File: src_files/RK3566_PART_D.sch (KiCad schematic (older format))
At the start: 16 parts

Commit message: littleupdate
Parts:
- removed U?: RK3566, symbol GCL_Integrated-Circuits:RK3566
- added C84, C85: 18pF, Capacitor_SMD:C_0402_1005Metric, symbol Device:C_Small
- added C86, C93: 100nF, Capacitor_SMD:C_0402_1005Metric, symbol Device:C_Small
- added R20, R21: 0R, Resistor_SMD:R_0402_1005Metric, symbol Device:R_US
- added U1: RK3566, greencharge-footprints:BGA828C65P31X31_2100X2100X161N, symbol GCL_Integrated-Circuits:RK3566
- added Y3: 24MHz/10ppm, Crystal:Crystal_SMD_3225-4Pin_3.2x2.5mm_HandSoldering, symbol Device:Crystal_GND24_Small
- C87, C88, C89, C90, C91, C92, C94, C95, C96, C97, C98: renamed from C?; footprint (none) -> Capacitor_SMD:C_0402_1005Metric
- R22, R23, R24: renamed from R?; footprint (none) -> Resistor_SMD:R_0402_1005Metric
- gave numbers to parts that had none: 1
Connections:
- net GND: now also C84.2, C85.2, C86.2, C93.2, U1.1D4 (DDR_AVSS), Y3.2, Y3.4
- net LPDDR4_A0_A: now also U1.C2 (LPDDR4_A0_A)
- net LPDDR4_A0_B: now also U1.A9 (LPDDR4_A0_B)
- net LPDDR4_A1_A: now also U1.C1 (LPDDR4_A1_A)
- net LPDDR4_A1_B: now also U1.B9 (LPDDR4_A1_B)
- net LPDDR4_A2_A: now also U1.1C1 (LPDDR4_A2_A)
- net LPDDR4_A2_B: now also U1.1B7 (LPDDR4_A2_B)
- net LPDDR4_A3_A: now also U1.1B3 (LPDDR4_A3_A)
- net LPDDR4_A3_B: now also U1.1B6 (LPDDR4_A3_B)
- net LPDDR4_A4_A: now also U1.1B1 (LPDDR4_A4_A)
- net LPDDR4_A4_B: now also U1.1A6 (LPDDR4_A4_B)
- net LPDDR4_A5_A: now also U1.1A1 (LPDDR4_A5_A)
- net LPDDR4_A5_B: now also U1.B8 (LPDDR4_A5_B)
- net LPDDR4_CKE0_A: now also U1.B4 (LPDDR4_CKE0_A)
- net LPDDR4_CKE0_B: now also U1.1A3 (LPDDR4_CKE0_B)
- net LPDDR4_CKE1_A: now also U1.1C3 (LPDDR4_CKE1)
- net LPDDR4_CKE1_B: now also U1.1A2 (LPDDR4_CKE1_B)
- net LPDDR4_CLKN_A: now also U1.A5 (LPDDR4_CLKN_A)
- net LPDDR4_CLKN_B: now also U1.B7 (LPDDR4_CLKN_B)
- net LPDDR4_CLKP_A: now also U1.B5 (LPDDR4_CLKP_A)
- net LPDDR4_CLKP_B: now also U1.A7 (LPDDR4_CLKP_B)
- net LPDDR4_CS0n_A: now also U1.B3 (LPDDR4_CS0n_A)
- net LPDDR4_CS0n_B: now also U1.1B5 (LPDDR4_CS0n_B)
- net LPDDR4_CS1n_A: now also U1.A3 (LPDDR4_CS1n_A)
- net LPDDR4_CS1n_B: now also U1.1A5 (LPDDR4_CS1n_B)
- net LPDDR4_DM0_A: now also U1.1E2 (LPDDR4_DM0_A)
- net LPDDR4_DM0_B: now also U1.1B8 (LPDDR4_DM0_B)
- net LPDDR4_DM1_A: now also U1.1G1 (LPDDR4_DM1_A)
- net LPDDR4_DM1_B: now also U1.1A11 (LPDDR4_DM1_B)
- net LPDDR4_DQ0_A: now also U1.G2 (DDR_DQ0_A/DDR4_DQL0_A/LPDDR4_DQ0_A/DDR3_DQ0/LPDDR3_DQ15)
- net LPDDR4_DQ0_B: now also U1.B12 (LPDDR4_DQ0_B)
- net LPDDR4_DQ10_A: now also U1.R2 (LPDDR4_DQ10_A)
- net LPDDR4_DQ10_B: now also U1.A20 (LPDDR4_DQ10_B)
- net LPDDR4_DQ11_A: now also U1.T2 (LPDDR4_DQ11_A)
- net LPDDR4_DQ11_B: now also U1.B20 (LPDDR4_DQ11_B)
- net LPDDR4_DQ12_A: now also U1.M1 (LPDDR4_DQ12_A)
- net LPDDR4_DQ12_B: now also U1.A15 (LPDDR4_DQ12_B)
- net LPDDR4_DQ13_A: now also U1.1F2 (LPDDR4_DQ13_A)
- net LPDDR4_DQ13_B: now also U1.B15 (LPDDR4_DQ13_B)
- net LPDDR4_DQ14_A: now also U1.1F1 (LPDDR4_DQ14_A)
- net LPDDR4_DQ14_B: now also U1.1C10 (LPDDR4_DQ14_B)
- net LPDDR4_DQ15_A: now also U1.1G2 (LPDDR4_DQ15_A)
- net LPDDR4_DQ15_B: now also U1.B16 (LPDDR4_DQ15_B)
- net LPDDR4_DQ1_A: now also U1.F2 (DDR_DQ1_A/DDR4_DQL2_A/LPDDR4_DQ1_A/DDR3_DQ1/LPDDR3_DQ14)
- net LPDDR4_DQ1_B: now also U1.B10 (LPDDR4_DQ1_B)
- net LPDDR4_DQ2_A: now also U1.F1 (DDR_DQ2_A/DDR4_DQL4_A/LPDDR4_DQ2_A/DDR3_DQ2/LPDDR3_DQ10)
- net LPDDR4_DQ2_B: now also U1.1A8 (LPDDR4_DQ2_B)
- net LPDDR4_DQ3_A: now also U1.E1 (DDR_DQ3_A/DDR4_DQL6_A//_LPDDR4_DQ3_A/DDR3_DQ3/LPDDR3_DQ9)
- net LPDDR4_DQ3_B: now also U1.1A7 (LPDDR4_DQ3_B)
- net LPDDR4_DQ4_A: now also U1.M2 (LPDDR4_DQ4_A)
- net LPDDR4_DQ4_B: now also U1.B13 (LPDDR4_DQ4_B)
- net LPDDR4_DQ5_A: now also U1.K1 (LPDDR4_DQ5_A)
- net LPDDR4_DQ5_B: now also U1.1A10 (LPDDR4_DQ5_B)
- net LPDDR4_DQ6_A: now also U1.K2 (LPDDR4_DQ6_A)
- net LPDDR4_DQ6_B: now also U1.1B9 (LPDDR4_DQ6_B)
- net LPDDR4_DQ7_A: now also U1.1E1 (LPDDR4_DQ7_A)
- net LPDDR4_DQ7_B: now also U1.1A9 (LPDDR4_DQ7_B)
- net LPDDR4_DQ8_A: now also U1.P2 (LPDDR4_DQ8_A)
- net LPDDR4_DQ8_B: now also U1.B19 (LPDDR4_DQ8_B)
- net LPDDR4_DQ9_A: now also U1.R1 (LPDDR4_DQ9_A)
- net LPDDR4_DQ9_B: now also U1.A19 (LPDDR4_DQ9_B)
- net LPDDR4_DQS0N_A: now also U1.H1 (LPDDR4_DQS0N_A)
- net LPDDR4_DQS0N_B: now also U1.A12 (LPDDR4_DQS0N_B)
- net LPDDR4_DQS0P_A: now also U1.H2 (LPDDR4_DQS0P_A)
- net LPDDR4_DQS0P_B: now also U1.A13 (LPDDR4_DQS0P_B)
- net LPDDR4_DQS1N_A: now also U1.N2 (LPDDR4_DQS1N_A)
- net LPDDR4_DQS1N_B: now also U1.B17 (LPDDR4_DQS1N_B)
- net LPDDR4_DQS1P_A: now also U1.N1 (LPDDR4_DQS1P_A)
- net LPDDR4_DQS1P_B: now also U1.A17 (LPDDR4_DQS1P_B)
- net LPDDR4_ODT0_CA_A: now also U1.E2 (LPDDR4_ODT0_CA_A)
- net LPDDR4_ODT0_CA_B: now also U1.A10 (LPDDR4_ODT0_CA_B)
- net LPDDR4_RESETn: now also U1.1C7 (LPDDR4_RESETn)
- net VCC_DDR: now also U1.1D5 (DDR_VDDQ_1), U1.1D6 (DDR_VDDQ_2), U1.1D7 (DDR_VDDQ_3), U1.1D8 (DDR_VDDQ_4), U1.1D9 (DDR_VDDQ_5), U1.1E4 (DDR_VDDQ_6), U1.1E6 (DDR_VDDQL_1), U1.1E7 (DDR_VDDQL_2), U1.1E9 (DDR_VDDQL_3), U1.1F4 (DDR_VDDQ_7), U1.1F5 (DDR_VDDQL_4), U1.1G4 (DDR_VDDQ_8), U1.1G5 (DDR_VDDQL_5)
- net at R22.2: now also U1.1F3 (DDR_RZQ)
- new net: C85.1, U1.AD37 (XIN24M), Y3.1
- new net: C84.1, U1.AD38 (XOUT24M), Y3.3
- new net: R20.1, U1.1M18 (TVSS)
- new net: R21.2, U1.1R20 (GPIO0_A1_z)
- new net GMAC1_RSTn_GPIO0_B7: U1.1R17 (GPIO0_B7_d)
- new net I2C0_SCL_PMIC: U1.AJ37 (GPIO0_B1_u)
- new net I2C0_SDA_PMIC: U1.AK38 (GPIO0_B2_u)
- new net I2C1_SCL: U1.AK37 (GPIO0_B3_u)
- new net I2C1_SDA: U1.AM38 (GPIO0_B4_u)
- new net I2C2_SCL_M0_TP: U1.1U20 (GPIO0_B5_u)
- new net I2C2_SDA_M0_TP: U1.1R16 (GPIO0_B6_u)
- new net PMIC_32KOUT_SOC: U1.1T20 (GPIO0_B0_u)
- new net PMIC_INT_L: U1.1R19 (GPIO0_A3_u)
- new net PMIC_SLEEP_H: U1.1P19 (GPIO0_A2_d)
- new net RESETn: C86.1, R21.1, U1.AG38 (nPOR_u)
- new net SDMMC0_DET_L: U1.AF37 (GPIO0_A4_u)
- new net TP_INT_GPIO0_A5: U1.AG37 (GPIO0_A5_d)
- new net USB_HOST5V_EN: U1.AJ38 (GPIO0_A6_d)
- new net VCC3V3_PMU: C93.1, U1.1P16 (PMUIO1)

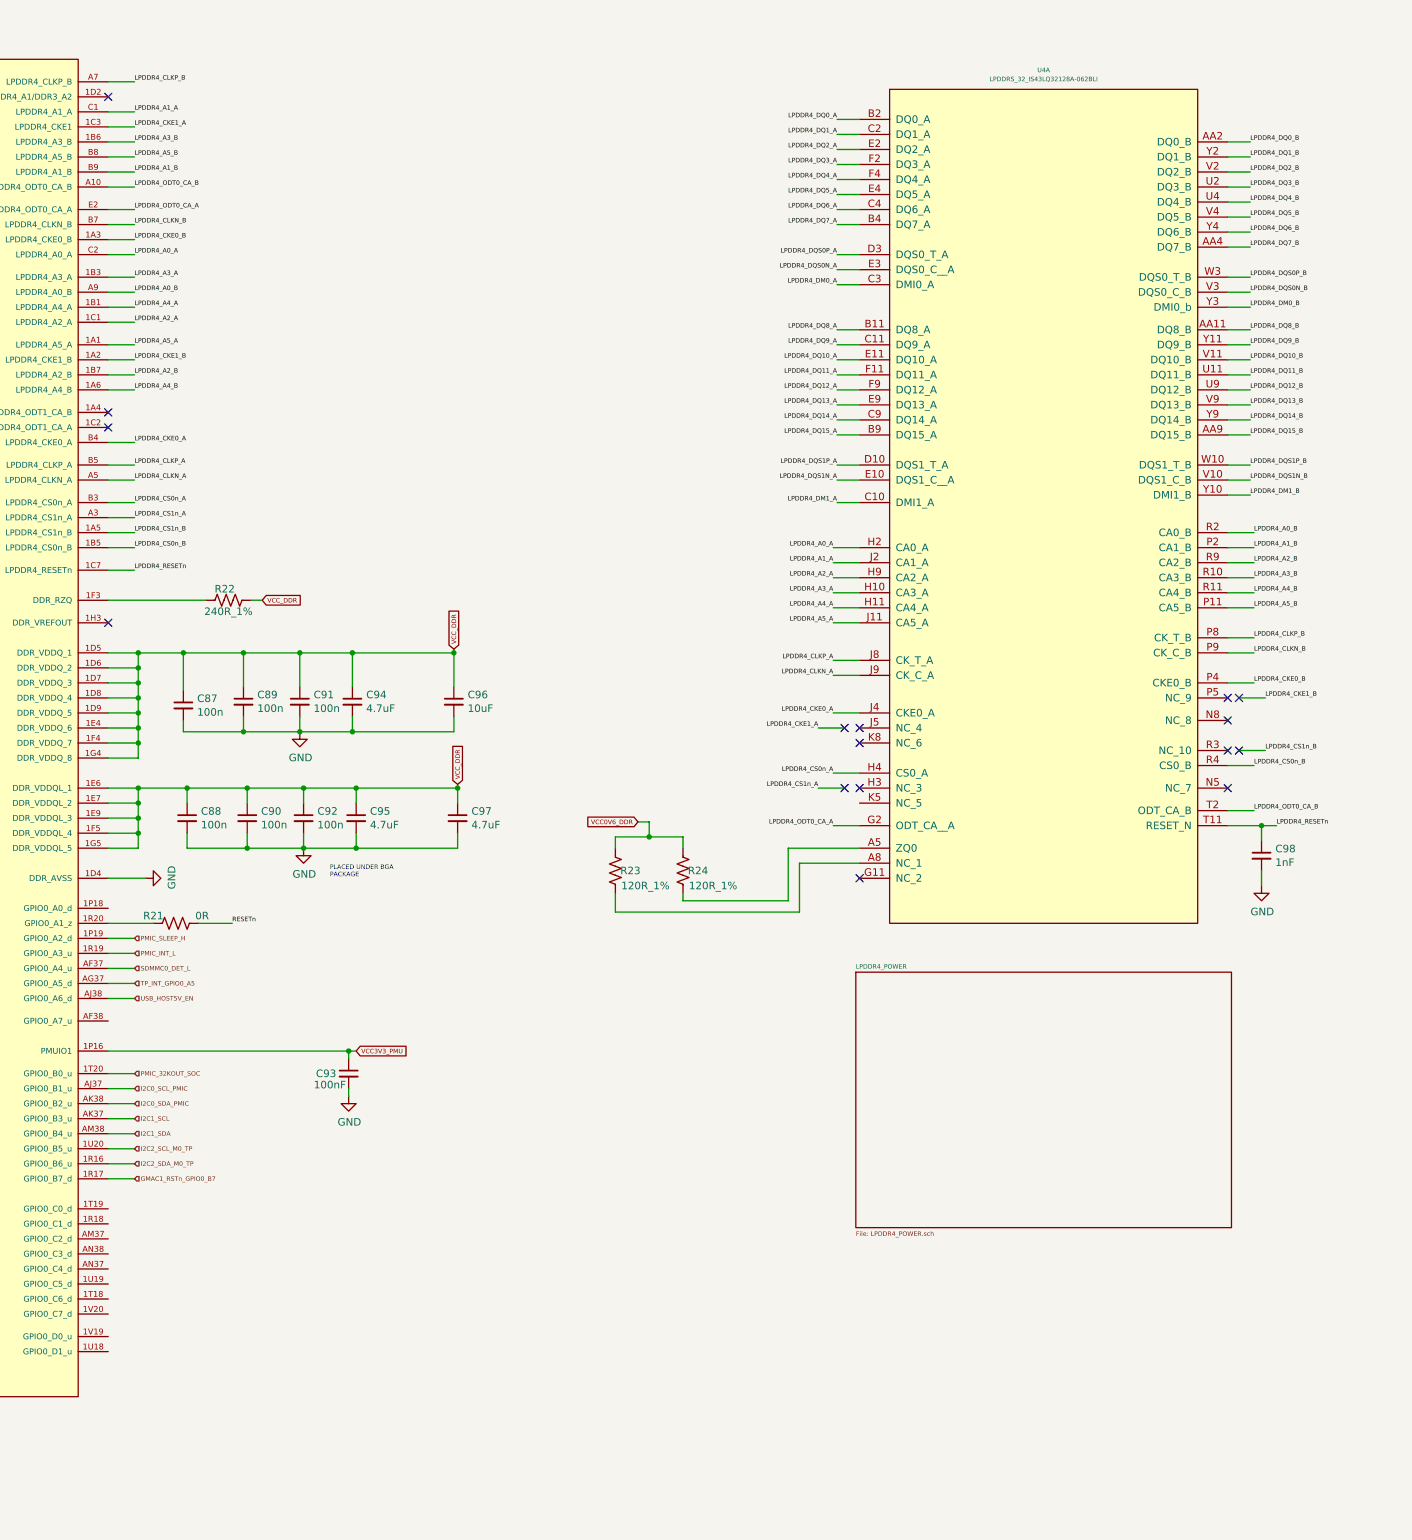
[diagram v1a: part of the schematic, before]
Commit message: added 3 screens
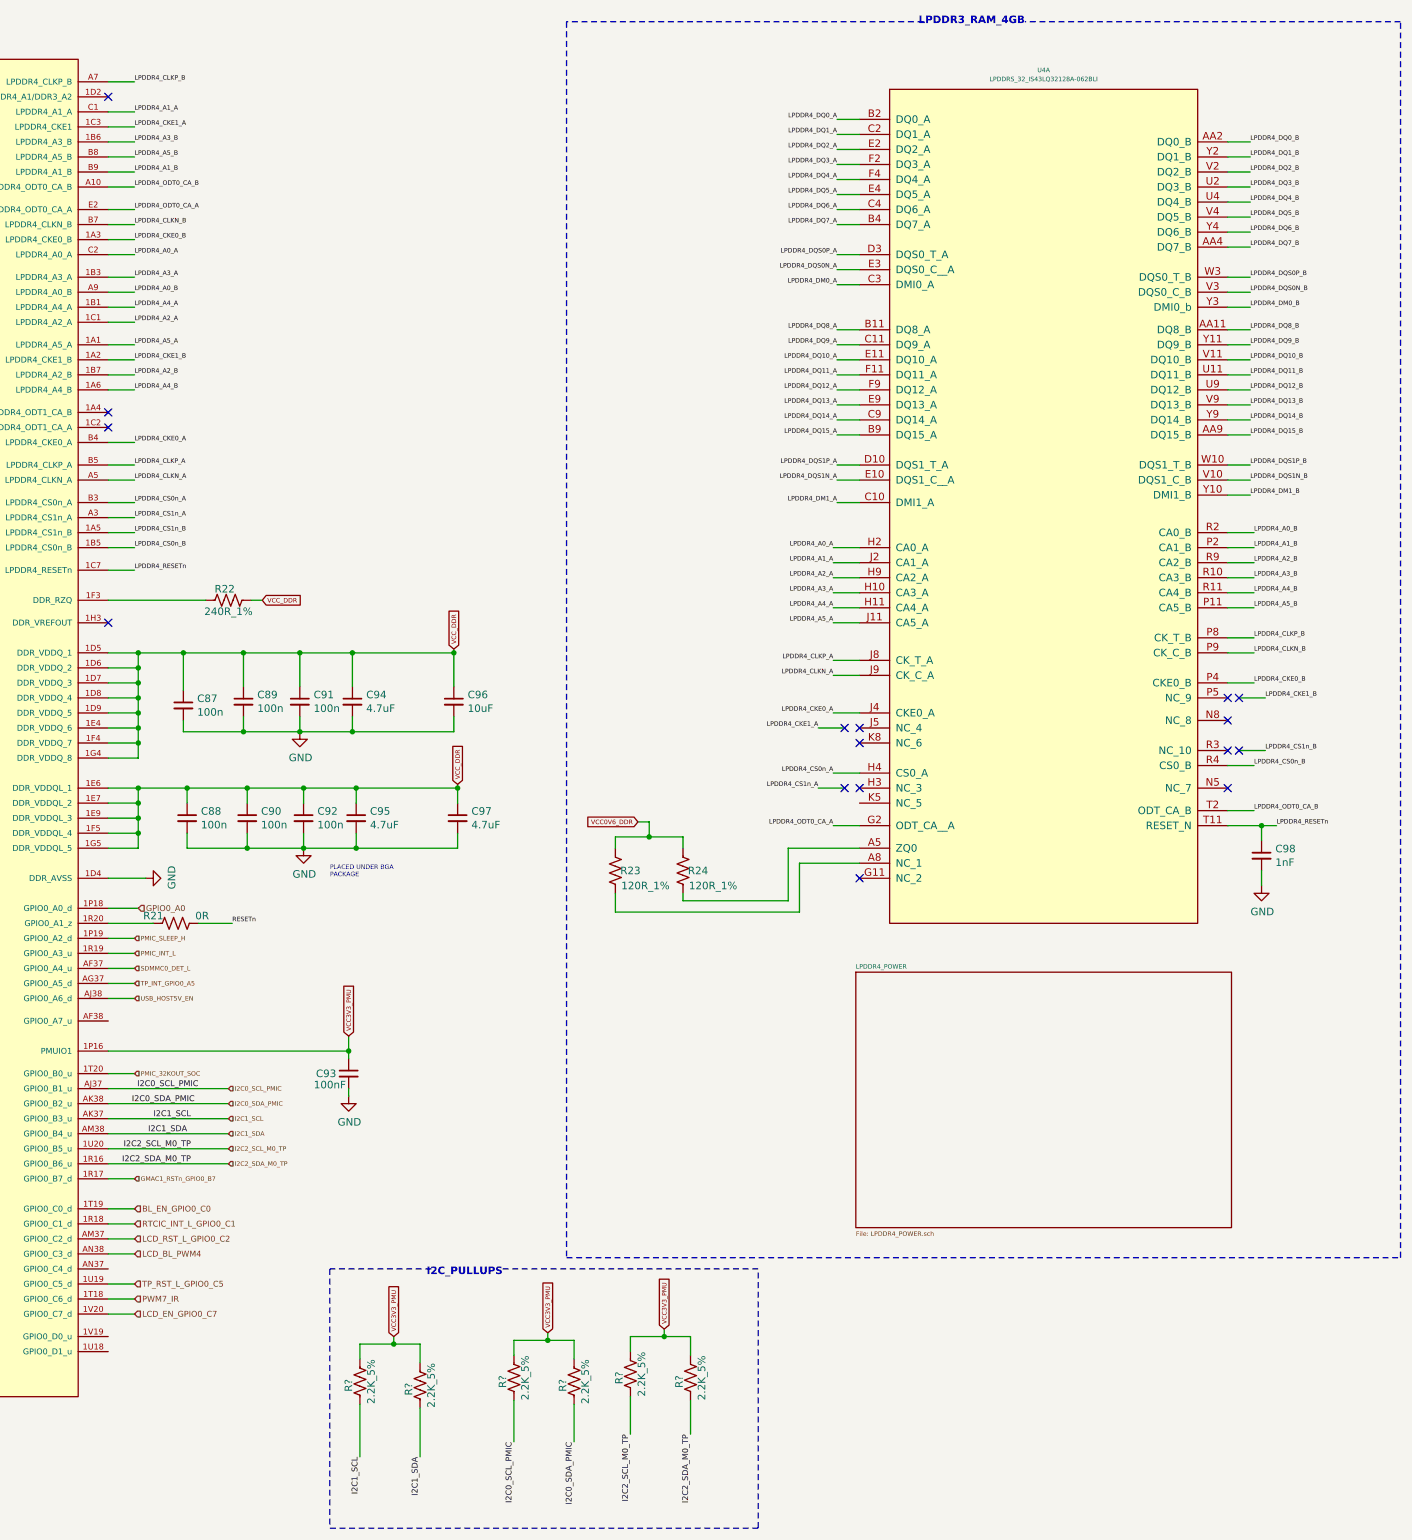
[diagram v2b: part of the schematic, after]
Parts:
- added R? (x6): 2.2K_5%, Resistor_SMD:R_0402_1005Metric, symbol Device:R_US
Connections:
- net I2C0_SCL_PMIC: now also R?.2
- net I2C0_SDA_PMIC: now also R?.2
- net I2C1_SCL: now also R?.2
- net I2C1_SDA: now also R?.2
- net I2C2_SCL_M0_TP: now also R?.2
- net I2C2_SDA_M0_TP: now also R?.2
- net VCC3V3_PMU: now also R?.1, R?.1, R?.1, R?.1, R?.1, R?.1
- net GPIO0_A0: now reaches U1.1P18 (GPIO0_A0_d)
- net RTCIC_INT_L_GPIO0_C1: now reaches U1.1R18 (GPIO0_C1_d)
- net PWM7_IR: now reaches U1.1T18 (GPIO0_C6_d)
- net BL_EN_GPIO0_C0: now reaches U1.1T19 (GPIO0_C0_d)
- net TP_RST_L_GPIO0_C5: now reaches U1.1U19 (GPIO0_C5_d)
- net LCD_EN_GPIO0_C7: now reaches U1.1V20 (GPIO0_C7_d)
- net LCD_RST_L_GPIO0_C2: now reaches U1.AM37 (GPIO0_C2_d)
- net LCD_BL_PWM4: now reaches U1.AN38 (GPIO0_C3_d)
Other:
- note added: "I2C_PULLUPS"
- note added: "LPDDR3_RAM_4GB"
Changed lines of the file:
@@
 $Descr A3 16535 11693
 encoding utf-8
-Sheet 8 11
+Sheet 10 11
 Title ""
 Date ""
@@
 Text HLabel 7425 7550 2    30   Input ~ 0
 USB_HOST5V_EN
-Text GLabel 8900 7900 2    30   Input ~ 0
+Text GLabel 8850 7800 1    30   Input ~ 0
 VCC3V3_PMU
-$Comp
-L Device:C_Small C93
-U 1 1 6340D3E8
-P 8850 8050
-F 0 "C93" H 8700 8050 50  0000 C CNN
-F 1 "100nF" H 8725 7975 50  0000 C CNN
-F 2 "Capacitor_SMD:C_0402_1005Metric" H 8850 8050 50  0001 C CNN
-F 3 "~" H 8850 8050 50  0001 C CNN
-	1    8850 8050
-	1    0    0    -1
-$EndComp
 $Comp
 L OLIMEX_Power:GND #PWR0191
@@
 	8850 8200 8850 8150
 Wire Wire Line
-	8850 7900 8900 7900
-Wire Wire Line
 	8850 7950 8850 7900
 Wire Wire Line
@@
 Text HLabel 7425 8050 2    30   Input ~ 0
 PMIC_32KOUT_SOC
-Text HLabel 7425 8150 2    30   Input ~ 0
+Text HLabel 8050 8150 2    30   Input ~ 0
 I2C0_SCL_PMIC
-Text HLabel 7425 8250 2    30   Input ~ 0
+Text HLabel 8050 8250 2    30   Input ~ 0
 I2C0_SDA_PMIC
-Text HLabel 7425 8350 2    30   Input ~ 0
+Text HLabel 8050 8350 2    30   Input ~ 0
 I2C1_SCL
-Text HLabel 7425 8450 2    30   Input ~ 0
+Text HLabel 8050 8450 2    30   Input ~ 0
 I2C1_SDA
-Text HLabel 7425 8550 2    30   Input ~ 0
-I2C2_SCL_M0_TP
-Text HLabel 7425 8650 2    30   Input ~ 0
-I2C2_SDA_M0_TP
 Text HLabel 7425 8750 2    30   Input ~ 0
 GMAC1_RSTn_GPIO0_B7
 Wire Wire Line
-	7425 8750 7250 8750
-Wire Wire Line
-	7425 8650 7250 8650
-Wire Wire Line
-	7425 8550 7250 8550
-Wire Wire Line
-	7425 8450 7250 8450
-Wire Wire Line
-	7425 8350 7250 8350
-Wire Wire Line
-	7425 8250 7250 8250
-Wire Wire Line
-	7425 8150 7250 8150
+	7425 8950 7250 8950
+Wire Wire Line
+	8050 8450 7250 8450
+Wire Wire Line
+	8050 8350 7250 8350
+Wire Wire Line
+	8050 8250 7250 8250
+Wire Wire Line
+	8050 8150 7250 8150
 Wire Wire Line
 	7425 8050 7250 8050
@@
 	1    0    0    -1
 $EndComp
+Text HLabel 7450 6950 2    39   Input ~ 0
+GPIO0_A0
+Wire Wire Line
+	7450 6950 7250 6950
+Text HLabel 7425 9650 2    39   Input ~ 0
+LCD_EN_GPIO0_C7
+Wire Wire Line
+	7250 9650 7425 9650
+Text HLabel 7425 8950 2    39   Input ~ 0
+BL_EN_GPIO0_C0
+Wire Wire Line
+	7425 8750 7250 8750
+Text HLabel 7425 9250 2    39   Input ~ 0
+LCD_BL_PWM4
+Text HLabel 7425 9150 2    39   Input ~ 0
+LCD_RST_L_GPIO0_C2
+Text HLabel 7425 9050 2    39   Input ~ 0
+RTCIC_INT_L_GPIO0_C1
+Wire Wire Line
+	7425 9050 7250 9050
+Wire Wire Line
+	7425 9150 7250 9150
+Wire Wire Line
+	7425 9250 7250 9250
+Text HLabel 7425 9450 2    39   Input ~ 0
+TP_RST_L_GPIO0_C5
+Text HLabel 7425 9550 2    39   Input ~ 0
+PWM7_IR
+Wire Wire Line
+	7425 9450 7250 9450
+Wire Wire Line
+	7425 9550 7250 9550
+Wire Wire Line
+	8850 7800 8850 7900
+$Comp
+L Device:C_Small C93
+U 1 1 6340D3E8
+P 8850 8050
+F 0 "C93" H 8700 8050 50  0000 C CNN
+F 1 "100nF" H 8725 7975 50  0000 C CNN
+F 2 "Capacitor_SMD:C_0402_1005Metric" H 8850 8050 50  0001 C CNN
+F 3 "~" H 8850 8050 50  0001 C CNN
+	1    8850 8050
+	1    0    0    -1
+$EndComp
+Wire Wire Line
+	9325 9850 9325 9975
+Wire Wire Line
+	8925 9950 8925 9850
+$Comp
+L Device:R_US R?
+U 1 1 6243D32E
+P 9325 10125
+F 0 "R?" V 9250 10100 50  0000 C CNN
+F 1 "2.2K_5%" V 9400 10125 50  0000 C CNN
+F 2 "Resistor_SMD:R_0402_1005Metric" V 9365 10115 50  0001 C CNN
+F 3 "~" H 9325 10125 50  0001 C CNN
+	1    9325 10125
+	1    0    0    -1
+$EndComp
+$Comp
+L Device:R_US R?
+U 1 1 62422541
+P 8925 10100
+F 0 "R?" V 8850 10075 50  0000 C CNN
+F 1 "2.2K_5%" V 9000 10100 50  0000 C CNN
+F 2 "Resistor_SMD:R_0402_1005Metric" V 8965 10090 50  0001 C CNN
+F 3 "~" H 8925 10100 50  0001 C CNN
+	1    8925 10100
+	1    0    0    -1
+$EndComp
+Wire Wire Line
+	8925 9850 9150 9850
+Text GLabel 9150 9800 1    30   Input ~ 0
+VCC3V3_PMU
+Wire Wire Line
+	9325 10275 9325 10600
+Wire Wire Line
+	8925 10250 8925 10600
+Wire Wire Line
+	8050 8550 7250 8550
+Wire Wire Line
+	8050 8650 7250 8650
+Text HLabel 8050 8650 2    30   Input ~ 0
+I2C2_SDA_M0_TP
+Text HLabel 8050 8550 2    30   Input ~ 0
+I2C2_SCL_M0_TP
+Text Label 7850 8150 2    39   ~ 0
+I2C0_SCL_PMIC
+Text Label 7825 8250 2    39   ~ 0
+I2C0_SDA_PMIC
+Text Label 7800 8350 2    39   ~ 0
+I2C1_SCL
+Text Label 7775 8450 2    39   ~ 0
+I2C1_SDA
+Text Label 7800 8550 2    39   ~ 0
+I2C2_SCL_M0_TP
+Text Label 7800 8650 2    39   ~ 0
+I2C2_SDA_M0_TP
+Text Label 11125 10450 3    39   ~ 0
+I2C2_SDA_M0_TP
+Text Label 10725 10450 3    39   ~ 0
+I2C2_SCL_M0_TP
+Text Label 9325 10600 3    39   ~ 0
+I2C1_SDA
+Text Label 8925 10600 3    39   ~ 0
+I2C1_SCL
+Wire Wire Line
+	10350 9825 10350 9950
+Wire Wire Line
+	9950 9925 9950 9825
+$Comp
+L Device:R_US R?
+U 1 1 626F2B0D
+P 10350 10100
+F 0 "R?" V 10275 10075 50  0000 C CNN
+F 1 "2.2K_5%" V 10425 10100 50  0000 C CNN
+F 2 "Resistor_SMD:R_0402_1005Metric" V 10390 10090 50  0001 C CNN
+F 3 "~" H 10350 10100 50  0001 C CNN
+	1    10350 10100
+	1    0    0    -1
+$EndComp
+$Comp
+L Device:R_US R?
+U 1 1 626F2B17
+P 9950 10075
+F 0 "R?" V 9875 10050 50  0000 C CNN
+F 1 "2.2K_5%" V 10025 10075 50  0000 C CNN
+F 2 "Resistor_SMD:R_0402_1005Metric" V 9990 10065 50  0001 C CNN
+F 3 "~" H 9950 10075 50  0001 C CNN
+	1    9950 10075
+	1    0    0    -1
+$EndComp
+Wire Wire Line
+	9950 9825 10175 9825
+Text GLabel 10175 9775 1    30   Input ~ 0
+VCC3V3_PMU
+Wire Wire Line
+	10350 10250 10350 10500
+Wire Wire Line
+	9950 10225 9950 10500
+Text Label 10350 10500 3    39   ~ 0
+I2C0_SDA_PMIC
+Text Label 9950 10500 3    39   ~ 0
+I2C0_SCL_PMIC
+Wire Wire Line
+	11125 9800 11125 9925
+Wire Wire Line
+	10725 9900 10725 9800
+$Comp
+L Device:R_US R?
+U 1 1 6277A9D8
+P 11125 10075
+F 0 "R?" V 11050 10050 50  0000 C CNN
+F 1 "2.2K_5%" V 11200 10075 50  0000 C CNN
+F 2 "Resistor_SMD:R_0402_1005Metric" V 11165 10065 50  0001 C CNN
+F 3 "~" H 11125 10075 50  0001 C CNN
+	1    11125 10075
+	1    0    0    -1
+$EndComp
+$Comp
+L Device:R_US R?
+U 1 1 6277A9E2
+P 10725 10050
+F 0 "R?" V 10650 10025 50  0000 C CNN
+F 1 "2.2K_5%" V 10800 10050 50  0000 C CNN
+F 2 "Resistor_SMD:R_0402_1005Metric" V 10765 10040 50  0001 C CNN
+F 3 "~" H 10725 10050 50  0001 C CNN
+	1    10725 10050
+	1    0    0    -1
+$EndComp
+Wire Wire Line
+	10725 9800 10950 9800
+Text GLabel 10950 9750 1    30   Input ~ 0
+VCC3V3_PMU
+Wire Wire Line
+	11125 10225 11125 10450
+Wire Wire Line
+	10725 10200 10725 10450
+Wire Wire Line
+	10950 9750 10950 9800
+Connection ~ 10950 9800
+Wire Wire Line
+	10950 9800 11125 9800
+Wire Wire Line
+	10175 9775 10175 9825
+Connection ~ 10175 9825
+Wire Wire Line
+	10175 9825 10350 9825
+Wire Wire Line
+	9150 9800 9150 9850
+Connection ~ 9150 9850
+Wire Wire Line
+	9150 9850 9325 9850
+Text Notes 13350 1075 2    50   ~ 10
+LPDDR3_RAM_4GB
+Wire Notes Line
+	12675 1050 10300 1050
+Wire Notes Line
+	10300 1050 10300 9275
+Wire Notes Line
+	10300 9275 15850 9275
+Wire Notes Line
+	15850 9275 15850 1050
+Wire Notes Line
+	15850 1050 13350 1050
+Text Notes 9875 9400 2    50   ~ 10
+I2C_PULLUPS
+Wire Notes Line
+	9400 9350 8725 9350
+Wire Notes Line
+	8725 9350 8725 11075
+Wire Notes Line
+	8725 11075 11575 11075
+Wire Notes Line
+	11575 11075 11575 9350
+Wire Notes Line
+	11575 9350 9875 9350
 $EndSCHEMATC
